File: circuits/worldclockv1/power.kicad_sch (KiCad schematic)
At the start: 28 parts, among them J3 Power, U3 LD1117S33TR_SOT223, U4 L7805, U5 L7805, U6 L7805

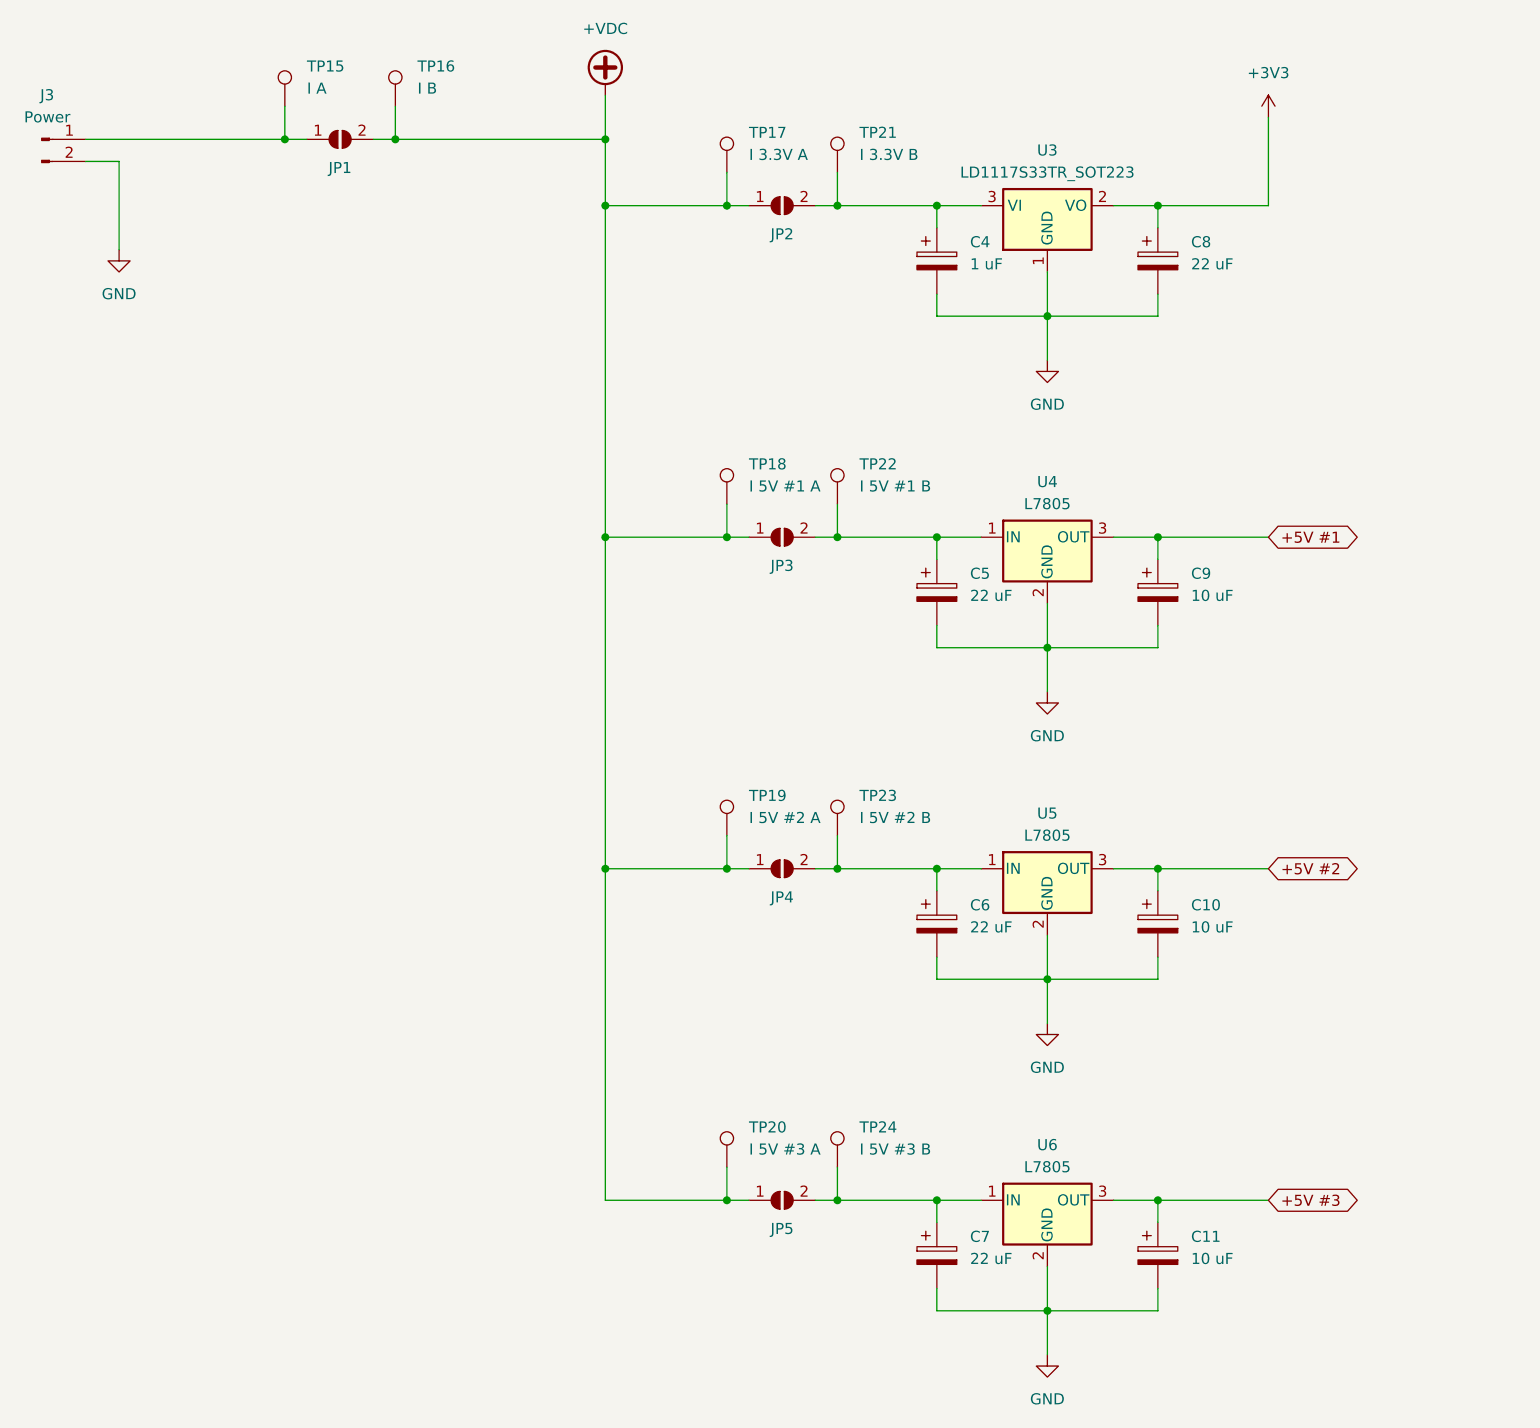
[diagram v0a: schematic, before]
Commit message: World Clock PCB completed
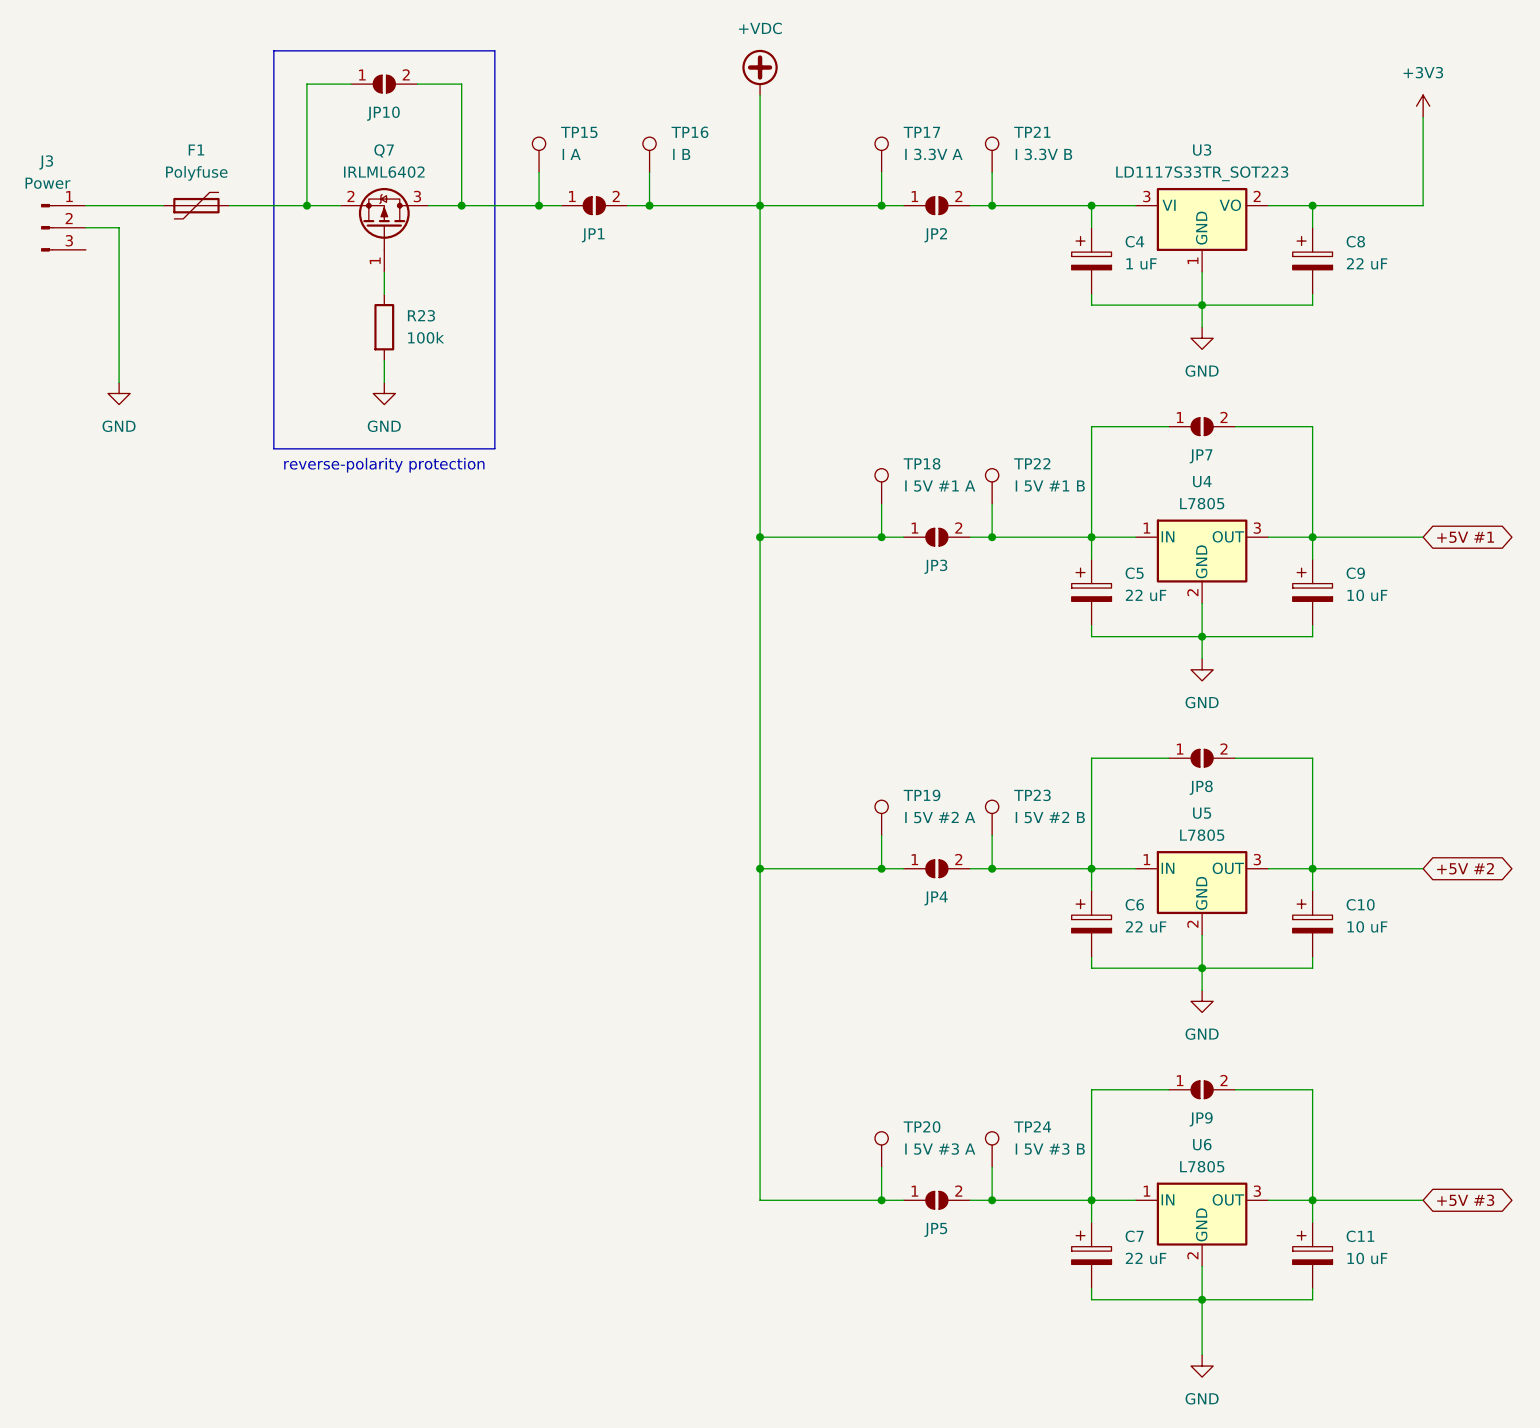
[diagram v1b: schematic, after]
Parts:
- removed J3: Power, Connector_PinSocket_2.54mm:PinSocket_1x02_P2.54mm_Vertical, symbol Connector:Conn_01x02_Pin
- added F1: Polyfuse, Fuse:Fuseholder_Littelfuse_Nano2_157x, symbol Device:Polyfuse
- added J3: Power, Connector_BarrelJack:BarrelJack_Horizontal, symbol Connector:Conn_01x03_Pin
- added JP10, JP7, JP8, JP9: ID_WP, Jumper:SolderJumper-2_P1.3mm_Open_RoundedPad1.0x1.5mm, symbol Jumper:SolderJumper_2_Open
- added Q7: IRLML6402, Package_TO_SOT_SMD:SOT-23, symbol Transistor_FET:IRLML6402
- added R23: 100k, Resistor_SMD:R_1206_3216Metric_Pad1.30x1.75mm_HandSolder, symbol Device:R
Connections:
- net +5V #1: now also JP7.2 (B)
- net +5V #2: now also JP8.2 (B)
- net +5V #3: now also JP9.2 (B)
- net GND: now also J3.2 (Pin_2), R23.2
- net at C5.1, JP3.2 (B), TP22.1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: now also JP7.1 (A)
- net at C7.1, JP5.2 (B), TP24.1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: now also JP9.1 (A)
- net at JP1.1 (A), TP15.1: now also JP10.2 (B), Q7.3 (D)
- net at C6.1, JP4.2 (B), TP23.1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: now also JP8.1 (A)
- new net: F1.1, J3.1 (Pin_1)
- new net: F1.2, JP10.1 (A), Q7.2 (S)
- new net: Q7.1 (G), R23.1
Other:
- note added: "reverse-polarity protection"
- moved on the sheet: C10, C11, C4, C5, C6, C7, C8, C9, JP1, JP2, JP3, JP4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

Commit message: Update some caps footprint sizes for the World Clock
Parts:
- C4, C5, C6, C7: footprint Capacitor_SMD:C_1206_3216Metric_Pad1.33x1.80mm_HandSolder -> Capacitor_SMD:CP_Elec_4x5.4
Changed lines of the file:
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@@
 			)
 		)
-		(property "Footprint" "Capacitor_SMD:C_1206_3216Metric_Pad1.33x1.80mm_HandSolder"
+		(property "Footprint" "Capacitor_SMD:CP_Elec_4x5.4"
 			(at 150.8252 48.26 0)
 			(effects
@@
 			)
 		)
-		(property "Footprint" "Capacitor_SMD:C_1206_3216Metric_Pad1.33x1.80mm_HandSolder"
+		(property "Footprint" "Capacitor_SMD:CP_Elec_4x5.4"
 			(at 150.8252 86.36 0)
 			(effects
@@
 			)
 		)
-		(property "Footprint" "Capacitor_SMD:C_1206_3216Metric_Pad1.33x1.80mm_HandSolder"
+		(property "Footprint" "Capacitor_SMD:CP_Elec_4x5.4"
 			(at 150.8252 124.46 0)
 			(effects
@@
 			)
 		)
-		(property "Footprint" "Capacitor_SMD:C_1206_3216Metric_Pad1.33x1.80mm_HandSolder"
+		(property "Footprint" "Capacitor_SMD:CP_Elec_4x5.4"
 			(at 150.8252 162.56 0)
 			(effects

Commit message: Update the footprint for the fuse and the layout on the PCB according for the World Clock
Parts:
- F1: footprint Fuse:Fuseholder_Littelfuse_Nano2_157x -> Fuse:Fuse_1812_4532Metric_Pad1.30x3.40mm_HandSolder
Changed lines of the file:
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@@
 			)
 		)
-		(property "Footprint" "Fuse:Fuseholder_Littelfuse_Nano2_157x"
+		(property "Footprint" "Fuse:Fuse_1812_4532Metric_Pad1.30x3.40mm_HandSolder"
 			(at 52.07 36.83 0)
 			(effects
